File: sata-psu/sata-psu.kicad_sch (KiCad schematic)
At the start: 25 parts, among them Q1 20V IN, Q2 5V OUT, Q3 5V OUT, U1 XL4015 (5V), U2 XL4015 (12V), U3 ACS758xCB-050B-PFF, U4 ACS758xCB-050B-PFF, U5 ESP32-C3_SUPERMINI_TH, U6 ACS712xLCTR-05B

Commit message: rework with ACS712
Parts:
- removed C1, C2: 50V 10nF, symbol Device:C
- removed C3, C4: 50V 100nF, symbol Device:C
- removed D1: P6KE6V8A, P6KE6V8A:DIOAD1300W80L670D310, symbol library:P6KE6V8A
- removed Q2: 5V OUT, XT60_YELLOW:AMASS_XT60PB-M, symbol library:XT60_YELLOW
- removed Q3: 5V OUT, XT60F, symbol library:XT60_YELLOW
- removed R1, R2: 100, symbol Device:R
- removed U3, U4: ACS758xCB-050B-PFF, Sensor_Current:Allegro_CB_PFF, symbol Sensor_Current:ACS758xCB-050B-PFF
- added C2, C3: 100uF, symbol Device:C_Polarized
- added C5, C8: 50V 1nF, symbol Device:C
- added C6, C7: 50V 100nF, symbol Device:C
- added D5: P6KE16A, P6KE16A:DIOAD1300W80L670D310, symbol library:P6KE16A
- added R10, R8: 2k, symbol Device:R
- added R7, R9: 1k, symbol Device:R
- added U7: ACS712xLCTR-05B, Package_SO:SOIC-8_3.9x4.9mm_P1.27mm, symbol Sensor_Current:ACS712xLCTR-05B
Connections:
- net +12V: now also U6.1 (IP+), U6.2 (IP+)
- net +5V: now also U6.8 (VCC), C6.2, C7.2, U7.1 (IP+), U7.2 (IP+), U7.8 (VCC)
- net 12V_CUR_SENSE: now also R10.2, R9.2
- net 5V_CUR_SENSE: now also R7.2, R8.2
- net GND: now also C2.2, C3.2, D5.A
- net 12V_OUT: now reaches D2.C
- net 12V_OUT: now also U6.3 (IP-), U6.4 (IP-), C2.1
- net at U6.5 (GND): now also C5.2, C6.1, R10.1
- net at U6.6 (FILTER): now also C5.1
- net at U6.7 (VIOUT): now also R9.1
- new net: C7.1, C8.2, R8.1, U7.5 (GND)
- new net: C8.1, U7.6 (FILTER)
- new net: R7.1, U7.7 (VIOUT)
- new net 5V_OUT: C3.1, D5.C, U7.3 (IP-), U7.4 (IP-)
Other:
- moved on the sheet: D3, F1, Q1, U1, U6

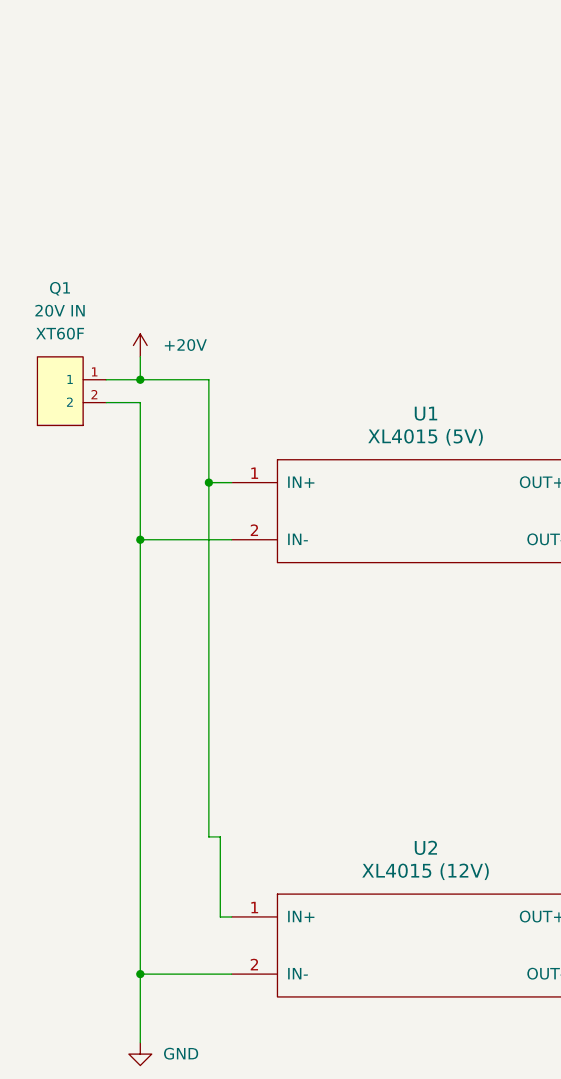
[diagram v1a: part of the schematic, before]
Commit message: sch: add 20V out
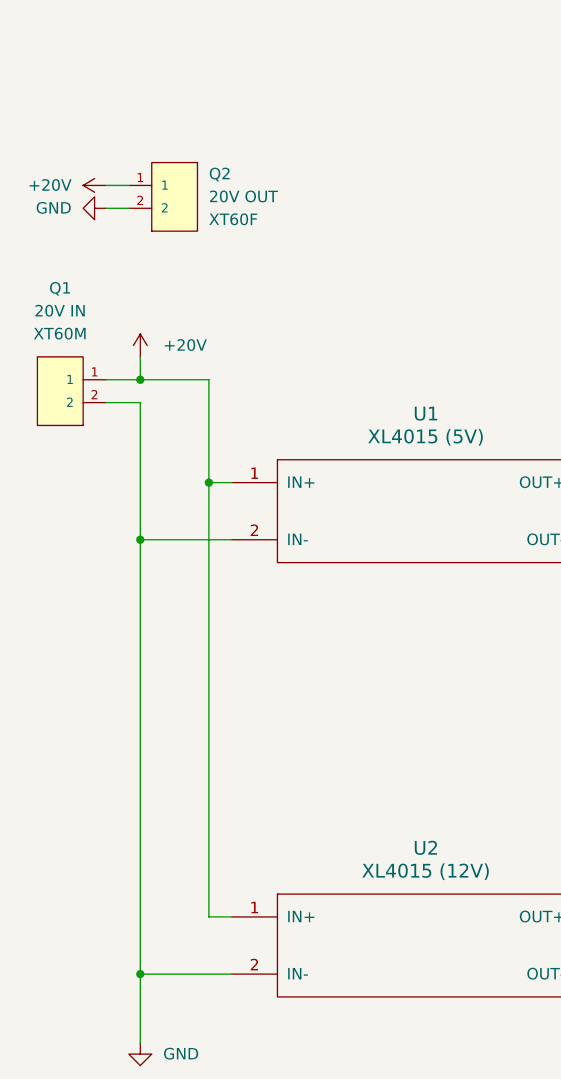
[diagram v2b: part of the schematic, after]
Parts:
- added Q2: 20V OUT, XT60_YELLOW:AMASS_XT60PB-M, symbol library:XT60_YELLOW
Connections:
- net +20V: now also Q2.1
- net GND: now also Q2.2
